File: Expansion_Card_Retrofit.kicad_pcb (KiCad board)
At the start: 2 copper layers, 24 x 27.3 mm, 40 parts, among them P1 USB_C_Plug_USB2.0, U1 RP2350_60QFN, U2 CCGM1A1, U4 W25X20CLUXIG-TR, U5 W25X20CLUXIG-TR, U6 NCP163AFCT330T2G, Y2 ABM8-272-T3

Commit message: update
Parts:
- removed D5, D6, D7, D8: 16-213SDRC/S530-A3/TR8, LED_SMD:LED_0402_1005Metric
- added C10: 100n, Capacitor_SMD:C_0402_1005Metric, F.Cu at (130.7, 141.0)
- added C100: 100n, Capacitor_SMD:C_0402_1005Metric, B.Cu at (138.9, 147.6)
- added C101: 100n, Capacitor_SMD:C_0402_1005Metric, B.Cu at (141.2, 147.5)
- added C102: 100n, Capacitor_SMD:C_0402_1005Metric, B.Cu at (141.2, 142.9)
- added C103: 100n, Capacitor_SMD:C_0402_1005Metric, B.Cu at (138.9, 146.7)
- added C104: 100n, Capacitor_SMD:C_0402_1005Metric, B.Cu at (141.2, 148.4)
- added C105: 100n, Capacitor_SMD:C_0402_1005Metric, B.Cu at (141.2, 142.0)
- added C106: 100n, Capacitor_SMD:C_0402_1005Metric, B.Cu at (138.9, 143.7)
- added C107: 1u, Capacitor_SMD:C_0402_1005Metric, B.Cu at (140.5, 145.1)
- added C108: 1u, Capacitor_SMD:C_0402_1005Metric, B.Cu at (141.6, 145.1)
- added C109: 1u, Capacitor_SMD:C_0402_1005Metric, B.Cu at (139.5, 145.1)
- added C11: 10n, Capacitor_SMD:C_0201_0603Metric, B.Cu at (130.5, 139.5)
- added C110: 1u, Capacitor_SMD:C_0402_1005Metric, B.Cu at (138.5, 145.1)
- added C111: 10n, Capacitor_SMD:C_0201_0603Metric, B.Cu at (137.3, 144.4)
- added C112: 10n, Capacitor_SMD:C_0201_0603Metric, B.Cu at (137.3, 146.0)
- added C113: 10n, Capacitor_SMD:C_0201_0603Metric, B.Cu at (142.9, 143.6)
- added C114: 10n, Capacitor_SMD:C_0201_0603Metric, B.Cu at (142.9, 144.4)
- added C115: 10n, Capacitor_SMD:C_0201_0603Metric, B.Cu at (142.9, 146.0)
- added C116: 10n, Capacitor_SMD:C_0201_0603Metric, B.Cu at (141.3, 143.8)
- added C117: 10n, Capacitor_SMD:C_0201_0603Metric, B.Cu at (141.3, 146.7)
- added C12: 100n, Capacitor_SMD:C_0402_1005Metric, B.Cu at (130.5, 140.3)
- added C13: 1u, Capacitor_SMD:C_0402_1005Metric, B.Cu at (130.5, 141.3)
- added C14: 1u, Capacitor_SMD:C_0402_1005Metric, B.Cu at (139.7, 135.4)
- added C15: 1u, Capacitor_SMD:C_0402_1005Metric, F.Cu at (139.8, 134.4)
- added C16: 10n, Capacitor_SMD:C_0201_0603Metric, B.Cu at (138.1, 149.2)
- added C17: 100n, Capacitor_SMD:C_0402_1005Metric, B.Cu at (139.2, 152.0)
- added C18: 1u, Capacitor_SMD:C_0402_1005Metric, B.Cu at (136.9, 152.1)
- added C19: 10n, Capacitor_SMD:C_0201_0603Metric, B.Cu at (139.3, 148.8)
- added C20: 10n, Capacitor_SMD:C_0201_0603Metric, B.Cu at (138.1, 148.4)
- added C21: 1u, Capacitor_SMD:C_0402_1005Metric, B.Cu at (144.2, 152.6)
- added C22: 100n, Capacitor_SMD:C_0402_1005Metric, B.Cu at (142.4, 152.0)
- added C23: 10n, Capacitor_SMD:C_0201_0603Metric, B.Cu at (142.9, 149.2)
- added C24: 10n, Capacitor_SMD:C_0201_0603Metric, B.Cu at (142.9, 148.4)
- added C25: 10n, Capacitor_SMD:C_0201_0603Metric, B.Cu at (141.3, 149.2)
- added C26: 1u, Capacitor_SMD:C_0402_1005Metric, B.Cu at (133.3, 143.5)
- added C27: 100n, Capacitor_SMD:C_0402_1005Metric, B.Cu at (136.1, 145.1)
- added C28: 10n, Capacitor_SMD:C_0201_0603Metric, B.Cu at (136.1, 143.3)
- added C29: 10n, Capacitor_SMD:C_0201_0603Metric, B.Cu at (133.3, 146.8)
- added C30: 10n, Capacitor_SMD:C_0201_0603Metric, B.Cu at (136.1, 147.2)
- added C31: 10n, Capacitor_SMD:C_0201_0603Metric, B.Cu at (136.5, 149.2)
- added C32: 10n, Capacitor_SMD:C_0201_0603Metric, B.Cu at (136.5, 148.4)
- added C33: 10n, Capacitor_SMD:C_0201_0603Metric, B.Cu at (134.5, 152.0)
- added C34: 100n, Capacitor_SMD:C_0402_1005Metric, B.Cu at (132.9, 151.9)
- added C35: 1u, Capacitor_SMD:C_0402_1005Metric, B.Cu at (133.3, 149.2)
- added C36: 10n, Capacitor_SMD:C_0201_0603Metric, B.Cu at (132.9, 140.6)
- added C37: 10n, Capacitor_SMD:C_0201_0603Metric, B.Cu at (137.3, 142.0)
- added C38: 10n, Capacitor_SMD:C_0201_0603Metric, B.Cu at (135.6, 140.4)
- added C39: 100n, Capacitor_SMD:C_0402_1005Metric, B.Cu at (140.0, 140.9)
- added C4: 4u7, Capacitor_SMD:C_0402_1005Metric, B.Cu at (139.6, 137.1)
- added C40: 1u, Capacitor_SMD:C_0402_1005Metric, B.Cu at (138.5, 141.4)
- added C41: 1u, Capacitor_SMD:C_0402_1005Metric, B.Cu at (141.9, 140.9)
- added C42: 100n, Capacitor_SMD:C_0402_1005Metric, F.Cu at (141.5, 136.2)
- added C43: 10n, Capacitor_SMD:C_0201_0603Metric, B.Cu at (140.5, 138.7)
- added C44: 10n, Capacitor_SMD:C_0201_0603Metric, B.Cu at (142.8, 139.6)
- added C45: 10n, Capacitor_SMD:C_0201_0603Metric, B.Cu at (143.2, 140.8)
- added C46: 10n, Capacitor_SMD:C_0201_0603Metric, B.Cu at (137.0, 130.6)
- added C47: 100n, Capacitor_SMD:C_0402_1005Metric, B.Cu at (135.8, 130.5)
- added C49: 10n, Capacitor_SMD:C_0201_0603Metric, F.Cu at (149.6, 151.1)
- added C5: 4u7, Capacitor_SMD:C_0402_1005Metric, B.Cu at (140.5, 137.1)
- added C50: 100n, Capacitor_SMD:C_0402_1005Metric, F.Cu at (149.6, 152.0)
- added C51: 1u, Capacitor_SMD:C_0402_1005Metric, F.Cu at (149.6, 153.0)
- added C52: 100n, Capacitor_SMD:C_0402_1005Metric, F.Cu at (111.7, 143.8)
- added C53: 10n, Capacitor_SMD:C_0201_0603Metric, B.Cu at (136.1, 139.2)
- added C54: 1u, Capacitor_SMD:C_0402_1005Metric, F.Cu at (99.2, 145.5)
- added C55: 100n, Capacitor_SMD:C_0402_1005Metric, F.Cu at (111.7, 145.8)
- added C56: 10n, Capacitor_SMD:C_0201_0603Metric, F.Cu at (99.2, 147.2)
- added C57: 1u, Capacitor_SMD:C_0402_1005Metric, B.Cu at (116.1, 146.3)
- added C58: 100n, Capacitor_SMD:C_0402_1005Metric, F.Cu at (111.7, 147.8)
- added C59: 10n, Capacitor_SMD:C_0201_0603Metric, F.Cu at (99.2, 150.7)
- added C6: 4u7, Capacitor_SMD:C_0402_1005Metric, B.Cu at (141.0, 139.8)
- added C60: 10n, Capacitor_SMD:C_0201_0603Metric, F.Cu at (99.2, 152.5)
- added C61: 10n, Capacitor_SMD:C_0201_0603Metric, F.Cu at (99.2, 154.2)
- added C62: 10n, Capacitor_SMD:C_0201_0603Metric, F.Cu at (101.7, 143.7)
- added C63: 10n, Capacitor_SMD:C_0201_0603Metric, B.Cu at (138.0, 138.8)
- added C64: 10n, Capacitor_SMD:C_0201_0603Metric, B.Cu at (134.1, 139.6)
- added C65: 1u, Capacitor_SMD:C_0402_1005Metric, B.Cu at (144.2, 144.8)
- added C66: 100n, Capacitor_SMD:C_0402_1005Metric, B.Cu at (146.9, 143.5)
- added C67: 10n, Capacitor_SMD:C_0201_0603Metric, B.Cu at (144.1, 143.2)
- added C68: 10n, Capacitor_SMD:C_0201_0603Metric, B.Cu at (146.8, 146.0)
- added C69: 10n, Capacitor_SMD:C_0201_0603Metric, B.Cu at (144.1, 146.5)
- added C70: 10n, Capacitor_SMD:C_0201_0603Metric, B.Cu at (144.1, 149.6)
- added C71: 10n, Capacitor_SMD:C_0201_0603Metric, B.Cu at (144.1, 148.0)
- added C72: 10n, Capacitor_SMD:C_0201_0603Metric, B.Cu at (146.9, 148.4)
- added C73: 100n, Capacitor_SMD:C_0402_1005Metric, B.Cu at (146.9, 150.7)
- added C74: 1u, Capacitor_SMD:C_0402_1005Metric, B.Cu at (146.9, 152.5)
- added C75: 10n, Capacitor_SMD:C_0201_0603Metric, B.Cu at (145.2, 141.2)
- added C76: 10n, Capacitor_SMD:C_0201_0603Metric, B.Cu at (147.5, 139.9)
- added C77: 10n, Capacitor_SMD:C_0201_0603Metric, B.Cu at (144.1, 140.8)
- added C78: 100n, Capacitor_SMD:C_0402_1005Metric, F.Cu at (145.8, 135.6)
- added C79: 1u, Capacitor_SMD:C_0402_1005Metric, F.Cu at (147.2, 135.8)
- added C80: 10n, Capacitor_SMD:C_0201_0603Metric, F.Cu at (144.4, 136.0)
- added C81: 1u, Capacitor_SMD:C_0402_1005Metric, F.Cu at (142.9, 135.2)
- added C82: 10n, Capacitor_SMD:C_0201_0603Metric, B.Cu at (134.5, 140.8)
- added C83: 4u7, Capacitor_SMD:C_0402_1005Metric, F.Cu at (130.0, 130.5)
- added C84: 22u, Capacitor_SMD:C_0402_1005Metric, F.Cu at (131.6, 132.9)
- added C85: 120p, Capacitor_SMD:C_0201_0603Metric, F.Cu at (132.5, 133.0)
- added C86: 4u7, Capacitor_SMD:C_0402_1005Metric, B.Cu at (130.0, 134.5)
- added C87: 120p, Capacitor_SMD:C_0201_0603Metric, B.Cu at (133.2, 132.7)
- added C88: 22u, Capacitor_SMD:C_0402_1005Metric, B.Cu at (131.6, 132.9)
- added C89: 100n, Capacitor_SMD:C_0402_1005Metric, B.Cu at (133.3, 137.9)
- added C9: 100n, Capacitor_SMD:C_0402_1005Metric, F.Cu at (130.6, 140.1)
- added C90: 1u, Capacitor_SMD:C_0402_1005Metric, B.Cu at (133.3, 136.9)
- added C91: 10n, Capacitor_SMD:C_0201_0603Metric, B.Cu at (137.3, 142.8)
- added C92: 10n, Capacitor_SMD:C_0201_0603Metric, B.Cu at (142.9, 142.0)
- added C93: 10n, Capacitor_SMD:C_0201_0603Metric, B.Cu at (137.3, 147.6)
- added C94: 10n, Capacitor_SMD:C_0201_0603Metric, B.Cu at (142.9, 146.8)
- added C95: 10n, Capacitor_SMD:C_0201_0603Metric, B.Cu at (137.3, 143.6)
- added C96: 10n, Capacitor_SMD:C_0201_0603Metric, B.Cu at (137.3, 146.8)
- added C97: 10n, Capacitor_SMD:C_0201_0603Metric, B.Cu at (142.9, 147.6)
- added C98: 10n, Capacitor_SMD:C_0201_0603Metric, B.Cu at (142.9, 142.8)
- added C99: 100n, Capacitor_SMD:C_0402_1005Metric, B.Cu at (138.9, 142.8)
- added D12: PTVS5V0Z1USK, Diode_SMD:Nexperia_DSN1608-2_1.6x0.8mm, F.Cu at (141.4, 132.3)
- added D13: PTVS5V0Z1USK, Diode_SMD:Nexperia_DSN1608-2_1.6x0.8mm, F.Cu at (141.4, 134.4)
- added JP1: Jumper_2_Open, Jumper:SolderJumper-2_P1.3mm_Open_RoundedPad1.0x1.5mm, F.Cu at (129.6, 153.3)
- added R1: 5K1, Resistor_SMD:R_0201_0603Metric, F.Cu at (139.0, 132.4)
- added R17: 5K1, Resistor_SMD:R_0201_0603Metric, F.Cu at (149.5, 137.0)
- added R18: 5K1, Resistor_SMD:R_0201_0603Metric, B.Cu at (148.0, 148.6)
- added R19: 5K1, Resistor_SMD:R_0201_0603Metric, B.Cu at (149.3, 153.9)
- added R2: 5K1, Resistor_SMD:R_0201_0603Metric, F.Cu at (135.0, 130.2)
- added R20: 5K1, Resistor_SMD:R_0201_0603Metric, B.Cu at (149.1, 148.9)
- added R21: 200R, Resistor_SMD:R_0201_0603Metric, F.Cu at (137.8, 135.8)
- added R22: 100R, Resistor_SMD:R_0201_0603Metric, F.Cu at (106.6, 152.5)
- added R23: 5K1, Resistor_SMD:R_0201_0603Metric, F.Cu at (155.3, 144.4)
- added R24: 316K, Resistor_SMD:R_0201_0603Metric, B.Cu at (132.4, 132.7)
- added R25: 200R, Resistor_SMD:R_0201_0603Metric, B.Cu at (132.2, 139.2)
- added R26: 0R, Resistor_SMD:R_0201_0603Metric, B.Cu at (132.2, 140.6)
- added R27: 0R, Resistor_SMD:R_0201_0603Metric, B.Cu at (131.9, 144.3)
- added R28: 200R, Resistor_SMD:R_0201_0603Metric, B.Cu at (131.8, 142.8)
- added R29: 0R, Resistor_SMD:R_0201_0603Metric, B.Cu at (134.6, 137.4)
- added R3: 33R, Resistor_SMD:R_0402_1005Metric, B.Cu at (139.6, 139.0)
- added R30: 0R, Resistor_SMD:R_0201_0603Metric, B.Cu at (134.1, 138.8)
- added R31: 100R, Resistor_SMD:R_0201_0603Metric, F.Cu at (109.0, 149.0)
- added R32: 0R, Resistor_SMD:R_0201_0603Metric, F.Cu at (130.6, 139.2)
- added R33: 0R, Resistor_SMD:R_0201_0603Metric, F.Cu at (130.6, 138.2)
- added R34: 0R, Resistor_SMD:R_0201_0603Metric, F.Cu at (109.0, 150.7)
- added R35: 100K, Resistor_SMD:R_0201_0603Metric, B.Cu at (132.1, 134.2)
- added R4: 5K1, Resistor_SMD:R_0201_0603Metric, F.Cu at (191.3, 113.4)
- added TH1: PTSLR06038V075, Capacitor_SMD:C_0603_1608Metric, F.Cu at (145.8, 130.3)
- added TP5: TestPoint_Small, TestPoint:TestPoint_Pad_D1.0mm, B.Cu at (151.2, 136.7)
- added TP6: TestPoint_Small, TestPoint:TestPoint_Pad_D1.0mm, B.Cu at (151.2, 138.8)
- added U3: TVS0500DRV, Package_SON:WSON-6-1EP_2x2mm_P0.65mm_EP1x1.6mm, F.Cu at (149.3, 131.1)
- added U7: TPSM82822SILR, ProjectLibrary:SIL0010D-MFG, F.Cu at (130.0, 132.6)
- added U8: TPSM82822SILR, ProjectLibrary:SIL0010D-MFG, B.Cu at (130.0, 132.6)
- added Y1: S3A2505-100.000-L-X1-R, ProjectLibrary:OSC_S3A2505-100.000-L-X1-R, B.Cu at (130.2, 137.2)
- C1, C2, C3: footprint Capacitor_SMD:C_0201_0603Metric -> Capacitor_SMD:C_0402_1005Metric
- C7, C8: value 100n -> 15p; footprint Capacitor_SMD:C_0201_0603Metric -> Capacitor_SMD:C_0402_1005Metric; moved to B.Cu
- P1: value USB_C_Plug_USB2.0 -> 1054440011
- R10, R11: value 60R4 -> 100K
- R12: value 60R4 -> 5K1
- R15: value 30R1 -> 5K1; moved to B.Cu
- R16: value 30R1 -> 0R; moved to B.Cu
- R9: value 60R4 -> 316K
- U4, U5: value W25X20CLUXIG-TR -> W25Q32RVXHJQ TR
- U6: value NCP163AFCT330T2G -> TPS7A2033PDQNR; footprint Package_CSP:WLCSP-4_0.64x0.64mm_P0.35mm -> Package_SON:Texas_X2SON-4_1x1mm_P0.65mm
- moved C8 38.4 mm to (150.4, 135.2)
- moved C7 38.0 mm to (150.2, 133.8), turned to 180 degrees
- moved D10 37.9 mm to (155.5, 141.4), turned to -90 degrees
- moved D11 36.7 mm to (154.2, 141.4), turned to 90 degrees
- moved R13 35.3 mm to (155.5, 139.5), turned to -90 degrees
- moved R14 34.2 mm to (154.2, 139.5), turned to -90 degrees
- moved R11 25.7 mm to (128.5, 133.4), turned to 90 degrees
- moved R16 24.7 mm to (135.2, 141.8), turned to -90 degrees
- moved C1 24.5 mm to (134.4, 131.0), turned to 180 degrees
- moved R10 23.9 mm to (131.9, 131.6), turned to 180 degrees
- moved U6 22.3 mm to (139.8, 135.7), turned to -90 degrees
- moved R9 21.3 mm to (133.2, 133.0), turned to 90 degrees
- moved R15 21.3 mm to (129.0, 139.8), turned to 90 degrees
- moved R12 10.2 mm to (129.7, 151.8)
- moved U5 9.53 mm to (149.1, 151.4)
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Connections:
- net /C_TX_N renamed /C_TX1_N
- net /C_TX_P renamed /C_TX1_P
- net /RX_N renamed /RX1_N
- net /RX_P renamed /RX1_P
- net Net-(D1-K) renamed /K0
- net Net-(D2-K) renamed /K1
- net Net-(D3-K) renamed /K2
- net Net-(D4-K) renamed /K3
- net Net-(U1-GPIO20) renamed /CC_CFG_CTRL_CLK
- net Net-(U1-GPIO22) renamed /CC_CFG_CTRL_VALID
- net Net-(U2C-IO_NA_A0) renamed /LED0
- C2 pad 1: /TX_N -> /TX1_N
- C3 pad 1: /TX_P -> /TX1_P
- D9 pad 2: /USB_DP -> /TX1_N
- D9 pad 4: VBUS -> /RX2_N
- D9 pad 5: /TX_P -> /TX2_N
- D9 pad 6: /TX_N -> /TX2_P
- D9 pad 7: Net-(D9-K6) -> /RX2_P
- D9 pad 8: /USB_DN -> /TX1_P
- P1 pad A10: unconnected-(P1-RX2--PadA10) -> /RX2_N
- P1 pad A11: unconnected-(P1-RX2+-PadA11) -> /RX2_P
- P1 pad A2: /TX_P -> /TX1_P
- P1 pad A3: /TX_N -> /TX1_N
- P1 pad A4: VBUS -> Net-(P1-VBUS-PadA4)
- P1 pad A5: Net-(D9-K6) -> Net-(P1-CC)
- P1 pad A9: VBUS -> Net-(P1-VBUS-PadA4)
- P1 pad B2: unconnected-(P1-TX2+-PadB2) -> /TX2_P
- P1 pad B3: unconnected-(P1-TX2--PadB3) -> /TX2_N
- P1 pad B4: VBUS -> Net-(P1-VBUS-PadA4)
- P1 pad B9: VBUS -> Net-(P1-VBUS-PadA4)
- R10 pad 1: Net-(U2C-IO_NA_A4) -> Net-(U7-FB)
- R10 pad 2: Net-(D6-K) -> GND
- R11 pad 1: Net-(U2C-IO_NA_B4) -> +2V5
- R11 pad 2: Net-(D7-K) -> /power_supply/PG
- R12 pad 1: Net-(U2C-IO_NA_A7) -> +2V5
- R12 pad 2: Net-(D8-K) -> Net-(JP1-B)
- R15 pad 1: Net-(Y1-CLK+) -> +2V5
- R15 pad 2: Net-(U2H-SER_CLK) -> Net-(Y1-ENABLE/DISABLE)
- R16 pad 1: Net-(Y1-CLK-) -> +1V
- R16 pad 2: Net-(U2H-SER_CLK_N) -> Net-(U2G-NC/VDD_SER)
- R6 pad 1: Net-(U2C-IO_NA_B0) -> /LED2
- R7 pad 1: Net-(U2C-IO_NA_A1) -> /LED4
- R8 pad 1: Net-(U2C-IO_NA_B1) -> /LED5
- R9 pad 1: Net-(U2C-IO_NA_A2) -> +2V5
- R9 pad 2: Net-(D5-K) -> Net-(U7-FB)
- U1 pad 33: Net-(U1-GPIO21) -> /GPIO21_GPOUT0
- U1 pad 35: Net-(U1-GPIO23) -> /GPIO22_GPOUT1
- U1 pad 36: unconnected-(U1-GPIO24-Pad36) -> /CC_CFG_CTRL_EN
- U1 pad 60: Net-(U1-QSPI_SS) -> Net-(JP1-B)
- U2 pad A4: Net-(U2C-IO_NA_A1) -> /LED2
- U2 pad A6: Net-(U2C-IO_NA_A4) -> /LED5
- U2 pad A8: Net-(U2C-IO_NA_A7) -> unconnected-(U2C-IO_NA_A7-PadA8)
- U2 pad B1: Net-(U1-GPIO21) -> /CC_CFG_CTRL_EN
- U2 pad B3: Net-(U2C-IO_NA_B0) -> unconnected-(U2C-IO_NA_B0-PadB3)
- U2 pad B4: Net-(U2C-IO_NA_B1) -> unconnected-(U2C-IO_NA_B1-PadB4)
- U2 pad B5: Net-(U2C-IO_NA_A2) -> /LED4
- U2 pad B6: Net-(U2C-IO_NA_B4) -> unconnected-(U2C-IO_NA_B4-PadB6)
- U2 pad D1: Net-(U1-GPIO23) -> unconnected-(U2F-IO_WC_A5-PadD1)
- U2 pad F9: +0V9 -> +1V
- U2 pad G10: +0V9 -> +1V
- U2 pad G12: +0V9 -> +1V
- U2 pad G6: +0V9 -> +1V
- U2 pad G8: +0V9 -> +1V
- U2 pad H11: +0V9 -> +1V
- U2 pad H13: +0V9 -> +1V
- U2 pad H7: +0V9 -> +1V
- U2 pad H9: +0V9 -> +1V
- U2 pad J10: +0V9 -> +1V
- U2 pad J12: +0V9 -> +1V
- U2 pad J6: +0V9 -> +1V
- U2 pad J8: +0V9 -> +1V
- U2 pad K11: +0V9 -> +1V
- U2 pad K13: +0V9 -> +1V
- U2 pad K18: unconnected-(U2D-IO_EA_A2-PadK18) -> /power_supply/PG
- U2 pad K7: +0V9 -> +1V
- U2 pad K9: +0V9 -> +1V
- U2 pad L10: +0V9 -> +1V
- U2 pad L12: +0V9 -> +1V
- U2 pad L6: +0V9 -> +1V
- U2 pad L8: +0V9 -> +1V
- U2 pad M11: +0V9 -> +1V
- U2 pad M13: +0V9 -> +1V
- U2 pad M7: +0V9 -> +1V
- U2 pad M9: +0V9 -> +1V
- U2 pad N10: +0V9 -> +1V
- U2 pad N16: unconnected-(U2G-NC-PadN16) -> Net-(U2G-NC/VDD_SER)
- U2 pad N18: +2V5 -> Net-(R27-Pad2)
- U2 pad N6: +0V9 -> +1V
- U2 pad N8: +0V9 -> +1V
- U2 pad P12: unconnected-(U2E-CLK1/IO_SB_A7-PadP12) -> /GPIO20_GPOUT0
- U2 pad P14: unconnected-(U2E-CLK2/IO_SB_A6-PadP14) -> /GPIO22_GPOUT1
- U2 pad P16: +0V9 -> +1V
- U2 pad R17: unconnected-(U2E-IO_SB_A1-PadR17) -> /C_TX2_N
- U2 pad R18: unconnected-(U2E-IO_SB_B1-PadR18) -> /C_TX2_P
- U2 pad T12: Net-(U2H-SER_CLK) -> /SER_CLK_P
- U2 pad T13: Net-(U2H-SER_CLK_N) -> /SER_CLK_N
- U2 pad T14: +2V5 -> +1V
- U2 pad T16: +0V9 -> +1V
- U2 pad T18: +2V5 -> Net-(R25-Pad2)
- U2 pad U1: unconnected-(U2B-POR_EN/IO_WA_A3-PadU1) -> /POR_EN
- U2 pad U12: +0V9 -> +1V
- U2 pad U16: GND -> Net-(U2A-GND/SER_TX1_P)
- U2 pad U17: unconnected-(U2E-IO_SB_A0-PadU17) -> /R_TX2_N
- U2 pad U18: unconnected-(U2E-IO_SB_B0-PadU18) -> /R_TX2_P
- U2 pad V12: unconnected-(U2A-SER_RTERM-PadV12) -> Net-(U2A-SER_RTERM)
- U2 pad V15: unconnected-(U2H-POR_ADJ-PadV15) -> Net-(U2H-POR_ADJ)
- U2 pad V16: GND -> Net-(U2A-GND/SER_TX1_N)
- U2 pad V17: +0V9 -> +1V
- U4 pad 1: Net-(U1-QSPI_SS) -> Net-(JP1-B)
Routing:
- net VBUS: track 2.61 -> 43.8 mm, vias 3 -> 8
- net +1V1: track 0.00 -> 28.3 mm, vias 0 -> 5
- net /TX2_N: track 0.00 -> 28.0 mm, vias 0 -> 2
- net /TX2_P: track 0.00 -> 27.6 mm, vias 0 -> 2
- net /RX2_N: track 0.00 -> 25.6 mm, vias 0 -> 2
- net /RX2_P: track 0.00 -> 24.8 mm, vias 0 -> 2
- net +1V: track 0.00 -> 19.5 mm, vias 0 -> 35
- net /HSTX_2_N: track 0.00 -> 19.0 mm, vias 0 -> 2
- net GND: track 46.5 -> 65.4 mm, vias 83 -> 98
- net +2V5: track 26.1 -> 44.4 mm, vias 46 -> 52
- net /HSTX_2_P: track 0.00 -> 18.0 mm, vias 0 -> 2
- net +0V9: track 17.0 -> 0.00 mm, vias 32 -> 0
- net /HSTX_0_N: track 0.00 -> 14.4 mm, vias 0 -> 2
- net /HSTX_3_N: track 0.00 -> 14.1 mm, vias 0 -> 1
- net /HSTX_3_P: track 0.00 -> 13.9 mm, vias 0 -> 1
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- added copper zone on B.Cu, net +1V
- added copper zone on B.Cu, net +1V1
- added copper zone on F.Cu, net +2V5
- added copper zone on B.Cu, net GND
- added copper zone on F.Cu, net GND
- added copper zone on In1.Cu, net GND
- added copper zone on In3.Cu, net GND
- added copper zone on In4.Cu, net GND
- added copper zone on In6.Cu, net GND
- added copper zone on B.Cu, net Net-(U1-VREG_LX)
- added copper zone on B.Cu, net VBUS
- added copper zone on F.Cu, net VBUS
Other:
- copper layers 2 -> 8

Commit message: first routing
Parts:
- removed C49: 10n, Capacitor_SMD:C_0201_0603Metric
- removed C50: 100n, Capacitor_SMD:C_0402_1005Metric
- removed C51: 1u, Capacitor_SMD:C_0402_1005Metric
- removed JP1: Jumper_2_Open, Jumper:SolderJumper-2_P1.3mm_Open_RoundedPad1.0x1.5mm
- removed R18, R19, R20: 5K1, Resistor_SMD:R_0201_0603Metric
- removed U5: W25Q32RVXHJQ TR, Package_SON:Winbond_USON-8-1EP_3x2mm_P0.5mm_EP0.2x1.6mm
- added D14: PTVS5V0Z1USK, Diode_SMD:Nexperia_DSN1608-2_1.6x0.8mm, F.Cu at (149.6, 149.3)
- added D15: PTVS5V0Z1USK, Diode_SMD:Nexperia_DSN1608-2_1.6x0.8mm, B.Cu at (148.3, 150.5)
- added D16: PTVS5V0Z1USK, Diode_SMD:Nexperia_DSN1608-2_1.6x0.8mm, B.Cu at (148.3, 148.4)
- added D5: 16-213SDRC/S530-A3/TR8, LED_SMD:LED_0402_1005Metric, B.Cu at (135.3, 153.7)
- added D6: 16-213SDRC/S530-A3/TR8, LED_SMD:LED_0402_1005Metric, B.Cu at (133.4, 153.7)
- added J1: Conn_02x02_Odd_Even, Connector_PinHeader_1.00mm:PinHeader_2x02_P1.00mm_Horizontal, F.Cu at (130.4, 151.7)
- added J3: 5024302030, Connector_Molex:Molex_SlimStack_502430-2010_2x10_P0.40mm_Vertical, F.Cu at (150.3, 140.5)
- added J4: Conn_02x02_Odd_Even, Connector_PinHeader_1.00mm:PinHeader_2x02_P1.00mm_Horizontal, F.Cu at (151.1, 151.7)
- added R36: 60R4, Resistor_SMD:R_0201_0603Metric, F.Cu at (135.5, 154.1)
- added R37: 60R4, Resistor_SMD:R_0201_0603Metric, F.Cu at (133.6, 154.1)
- added R38: 0R, Resistor_SMD:R_0201_0603Metric, B.Cu at (149.9, 139.7)
- added R39: 0R, Resistor_SMD:R_0201_0603Metric, B.Cu at (149.9, 138.9)
- C14: moved to F.Cu
- C52, D10, D11, R12, R22, R31, R34, R4: moved to B.Cu
- moved R4 62.0 mm to (135.3, 139.9), turned to 90 degrees
- moved C61 52.1 mm to (146.3, 131.8), turned to -90 degrees
- moved C60 51.8 mm to (147.5, 133.6), turned to 180 degrees
- moved C59 50.6 mm to (147.7, 136.3), turned to 180 degrees
- moved C56 50.2 mm to (147.8, 134.8), turned to 90 degrees
- moved C54 47.1 mm to (144.4, 131.9), turned to -90 degrees
- moved C62 43.1 mm to (143.0, 131.3)
- moved R34 40.4 mm to (147.8, 139.6), turned to 180 degrees
- moved C58 37.3 mm to (145.5, 132.0), turned to -90 degrees
- moved C57 36.7 mm to (149.7, 131.4), turned to 90 degrees
- moved C55 34.2 mm to (144.3, 135.8), turned to 90 degrees
- moved R22 32.3 mm to (135.3, 137.7), turned to 90 degrees
- moved R31 28.4 mm to (133.9, 135.2)
- moved C52 23.5 mm to (133.9, 136.0), turned to 180 degrees
- moved R17 22.9 mm to (130.4, 149.6), turned to -90 degrees
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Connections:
- net Net-(JP1-B) renamed /~{FLASH_CS}
- net Net-(U1-QSPI_SCLK) renamed /FLASH_CLK
- net Net-(U1-QSPI_SD0) renamed /FLASH_S0
- net Net-(U1-QSPI_SD1) renamed /FLASH_S1
- net Net-(U1-QSPI_SD2) renamed /FLASH_S2
- net Net-(U1-QSPI_SD3) renamed /FLASH_S3
- R6 pad 1: /LED2 -> /LED1
- R7 pad 1: /LED4 -> /LED2
- R8 pad 1: /LED5 -> /LED3
- U1 pad 33: /GPIO21_GPOUT0 -> unconnected-(U1-GPIO21-Pad33)
- U1 pad 35: /GPIO22_GPOUT1 -> /GPIO23_GPOUT1
- U2 pad A12: unconnected-(U2C-IO_NB_B4-PadA12) -> /LED2
- U2 pad A14: unconnected-(U2C-IO_NB_B7-PadA14) -> /LED4
- U2 pad A3: /LED0 -> unconnected-(U2C-IO_NA_A0-PadA3)
- U2 pad A4: /LED2 -> unconnected-(U2C-IO_NA_A1-PadA4)
- U2 pad A6: /LED5 -> unconnected-(U2C-IO_NA_A4-PadA6)
- U2 pad A8: unconnected-(U2C-IO_NA_A7-PadA8) -> /LED0
- U2 pad A9: unconnected-(U2C-IO_NB_B0-PadA9) -> /LED1
- U2 pad B12: unconnected-(U2C-IO_NB_A4-PadB12) -> /LED3
- U2 pad B14: unconnected-(U2C-IO_NB_A7-PadB14) -> /LED5
- U2 pad B5: /LED4 -> unconnected-(U2C-IO_NA_A2-PadB5)
- U2 pad C17: unconnected-(U2D-IO_EB_B4-PadC17) -> /RX1
- U2 pad C18: unconnected-(U2D-IO_EB_A4-PadC18) -> /RX0
- U2 pad D17: unconnected-(U2D-IO_EB_B2-PadD17) -> /TX1
- U2 pad D18: unconnected-(U2D-IO_EB_A2-PadD18) -> /TX0
- U2 pad E3: unconnected-(U2F-IO_WC_A4-PadE3) -> /IO_P
- U2 pad E4: unconnected-(U2F-IO_WC_B4-PadE4) -> /IO_N
- U2 pad L3: /TX1 -> unconnected-(U2F-IO_WB_A2-PadL3)
- U2 pad L4: /RX1 -> unconnected-(U2F-IO_WB_B2-PadL4)
- U2 pad M3: /TX0 -> unconnected-(U2F-IO_WB_A1-PadM3)
- U2 pad M4: /RX0 -> unconnected-(U2F-IO_WB_B1-PadM4)
- U2 pad P12: /GPIO20_GPOUT0 -> /GPIO23_GPOUT1
- U2 pad P14: /GPIO22_GPOUT1 -> unconnected-(U2E-CLK2/IO_SB_A6-PadP14)
- U2 pad U4: GND -> /CFG_MD2/IO_WA_A1
- U2 pad V4: GND -> /CFG_MD3/IO_WA_B1
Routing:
- net /~{RST}: track 0.57 -> 65.9 mm, vias 1 -> 2
- net GND: track 65.4 -> 107.6 mm, vias 98 -> 108
- net /~{FLASH_CS}: track 2.04 -> 38.2 mm, vias 0 -> 2
- net /RUN: track 0.00 -> 33.0 mm, vias 0 -> 1
- net /TX1: track 0.57 -> 31.0 mm, vias 1 -> 2
- net /CC_CFG_CTRL_VALID: track 0.57 -> 26.7 mm, vias 1 -> 2
- net +2V5: track 44.4 -> 70.4 mm, vias 52 -> 54
- net /RX1: track 0.57 -> 25.5 mm, vias 1 -> 2
- net Net-(U2B-IO_WA_B2/CFG_DONE): track 3.13 -> 26.9 mm, vias 0 -> 2
- net /RX0: track 0.57 -> 24.1 mm, vias 1 -> 2
- net /TX0: track 0.57 -> 23.9 mm, vias 1 -> 2
- net /CC_CFG_CTRL_EN: track 0.57 -> 21.3 mm, vias 1 -> 2
- net /TCK: track 0.57 -> 18.4 mm, vias 1 -> 2
- net /CC_CFG_CTRL_CLK: track 0.57 -> 18.1 mm, vias 1 -> 2
- net Net-(U2B-IO_WA_A2/~{CFG_FAILED}): track 2.17 -> 19.2 mm, vias 0 -> 4
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
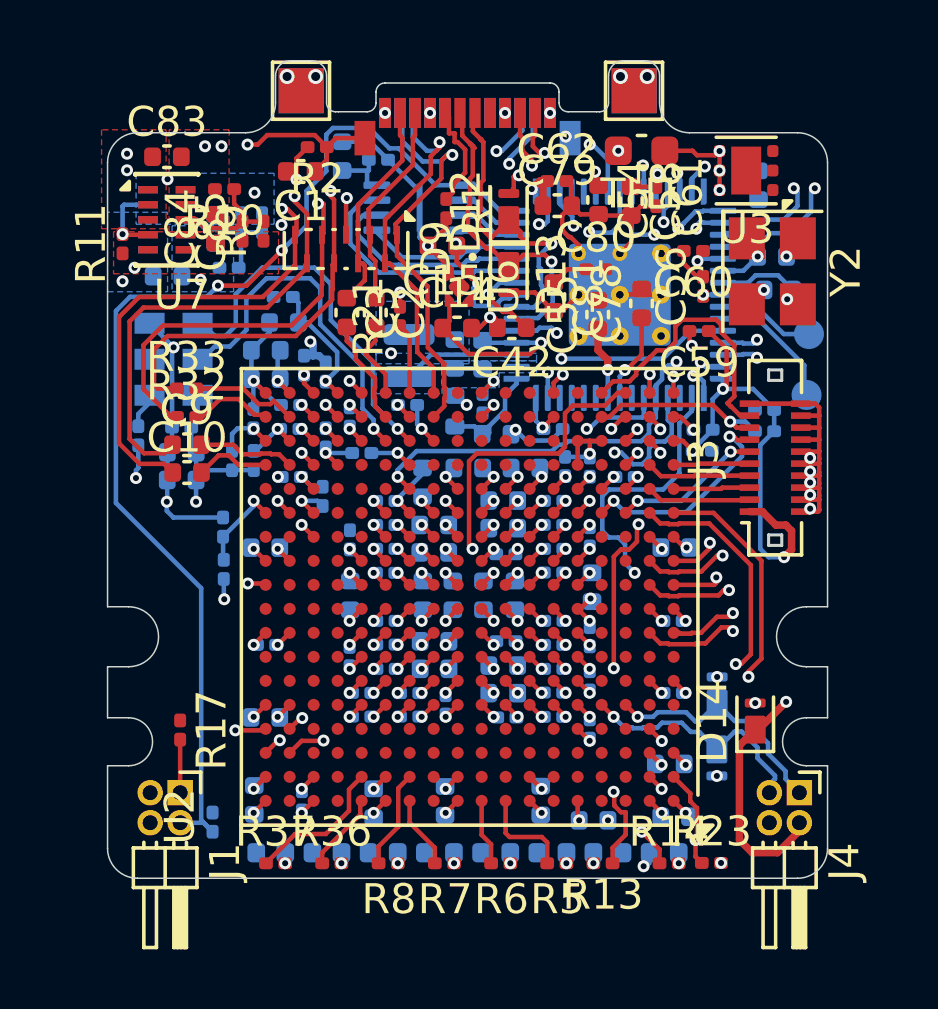
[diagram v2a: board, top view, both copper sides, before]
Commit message: Layout and add sensor
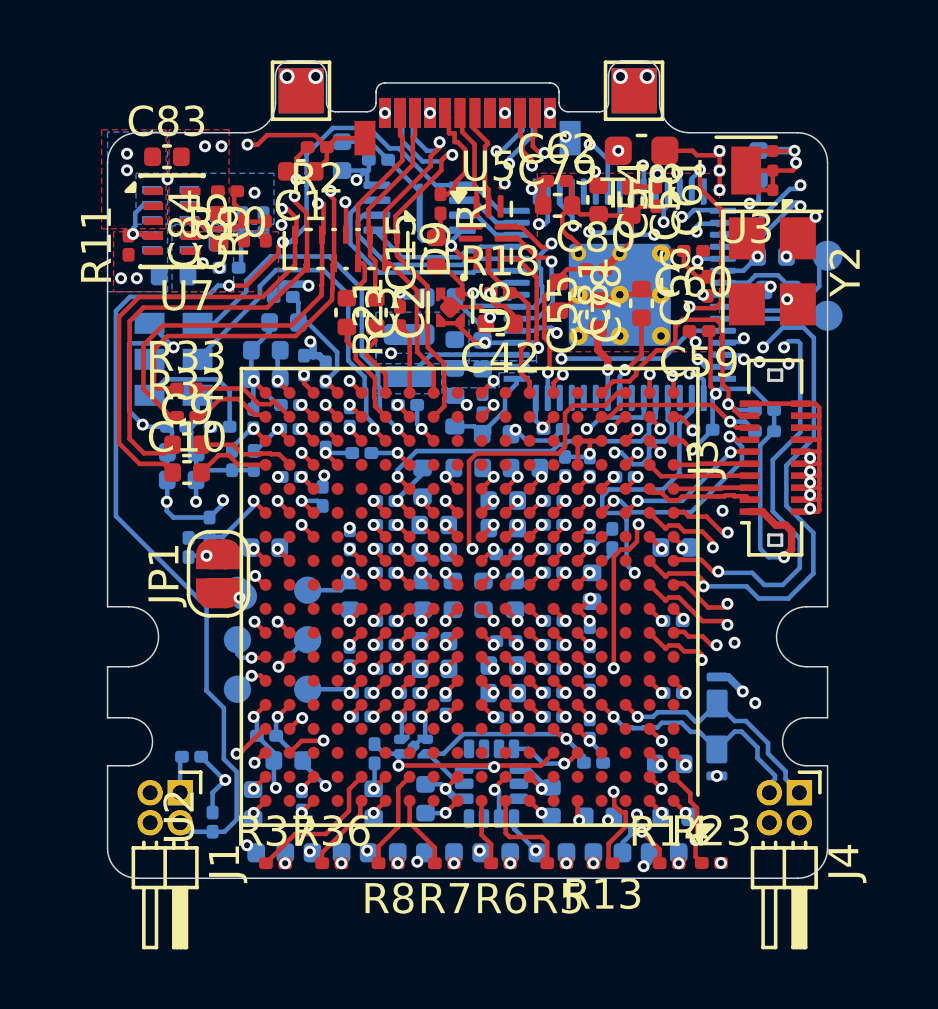
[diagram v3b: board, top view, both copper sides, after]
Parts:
- removed D12, D13, D14: PTVS5V0Z1USK, Diode_SMD:Nexperia_DSN1608-2_1.6x0.8mm
- added JP1: Jumper_2_Small_Open, Jumper:SolderJumper-2_P1.3mm_Open_RoundedPad1.0x1.5mm, F.Cu at (131.7, 144.4)
- added MK1: CMM-4737DT-26386-TR, Sensor_Audio:ST_HLGA-6_3.76x4.72mm_P1.65mm, B.Cu at (133.5, 146.6)
- added R18: 5K1, Resistor_SMD:R_0201_0603Metric, F.Cu at (141.1, 135.0)
- added R19: 5K1, Resistor_SMD:R_0201_0603Metric, B.Cu at (136.9, 150.4)
- added R20: 5K1, Resistor_SMD:R_0201_0603Metric, B.Cu at (144.2, 150.7)
- added U10: TMP110D, Package_SON:Texas_X2SON-5_0.8x0.8mm_P0.48mm, B.Cu at (138.2, 150.2)
- added U5: USB3740B-AI2, Package_DFN_QFN:UQFN-10_1.3x1.8mm_P0.4mm, F.Cu at (140.7, 133.0)
- added U9: ISM330DHCX, Package_LGA:LGA-14_3x2.5mm_P0.5mm_LayoutBorder3x4y, B.Cu at (140.8, 151.4)
- C14, R17: moved to B.Cu
- U4: value W25Q32RVXHJQ TR -> W25Q16JLUXIG TR
- moved C76 4.19 mm to (144.8, 143.2), turned to 90 degrees
- moved C29 3.03 mm to (133.3, 149.8)
- moved R15 2.74 mm to (131.8, 139.5), turned to 0 degrees
- moved TP6 2.73 mm to (152.0, 135.8)
- moved TP5 2.68 mm to (152.0, 133.8)
- moved C35 1.63 mm to (134.0, 150.6)
- moved R27 1.38 mm to (130.7, 143.5)
- moved C14 1.16 mm to (139.1, 135.2), turned to 180 degrees
- moved R17 0.97 mm to (130.8, 150.5), turned to 180 degrees
- moved U6 0.74 mm to (139.4, 135.5)
- moved C57 0.67 mm to (149.7, 130.8)
- moved C17 0.65 mm to (138.6, 151.9)
- moved R28 0.45 mm to (131.4, 142.8)
- moved C42 0.41 mm to (141.1, 136.1)
- moved C22 0.36 mm to (142.8, 152.0)
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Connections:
- net /K5 renamed /K8
- J4 pad 2: +2V5 -> GND
- P1 pad A6: /USB_DN -> /C_USB_DP
- P1 pad A7: /USB_DP -> /C_USB_DN
- U2 pad B8: unconnected-(U2C-IO_NA_B7-PadB8) -> /IMU_INT2
- U2 pad C5: unconnected-(U2C-IO_NA_B2-PadC5) -> /IMU_INT1
- U2 pad C6: unconnected-(U2C-IO_NA_A3-PadC6) -> /SDA0
- U2 pad D6: unconnected-(U2C-IO_NA_B3-PadD6) -> /SCL0
- U2 pad F18: unconnected-(U2D-IO_EB_A0-PadF18) -> /MIC_CLK
- U2 pad G17: unconnected-(U2D-IO_EA_B7-PadG17) -> /MIC_LR
- U2 pad G18: unconnected-(U2D-IO_EA_A7-PadG18) -> /MIC_DOUT
- U2 pad H1: /HSTX_3_P -> /HSTX_1_P
- U2 pad H2: /HSTX_3_N -> /HSTX_1_N
- U2 pad L1: /HSTX_1_P -> /HSTX_0_P
- U2 pad L2: /HSTX_1_N -> /HSTX_0_N
- U2 pad N1: /HSTX_0_P -> /HSTX_3_P
- U2 pad N2: /HSTX_0_N -> /HSTX_3_N
- U2 pad V7: unconnected-(U2E-IO_SA_B3-PadV7) -> /D_EN
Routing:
- net GND: track 107.6 -> 129.1 mm, vias 108 -> 119
- net /HSTX_1_P: track 5.08 -> 23.7 mm
- net /HSTX_1_N: track 7.10 -> 24.7 mm
- net /HSTX_0_N: track 8.78 -> 23.4 mm, vias 2 -> 3
- net +3V3: track 6.79 -> 21.0 mm, vias 4 -> 3
- net /HSTX_0_P: track 9.37 -> 21.9 mm, vias 2 -> 3
- net +2V5: track 70.4 -> 80.5 mm, vias 54 -> 68
- net /SCL0: track 0.00 -> 8.36 mm, vias 0 -> 1
- net /SDA0: track 0.00 -> 7.90 mm, vias 0 -> 2
- net /USB_DN: track 11.1 -> 4.66 mm
- net /USB_DP: track 10.6 -> 4.89 mm
- net /D_EN: track 0.00 -> 5.37 mm
- net /HSTX_2_N: track 18.1 -> 13.9 mm
- net /C_USB_DN: track 0.00 -> 3.44 mm
- net /C_USB_DP: track 0.00 -> 3.34 mm
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- added copper zone on In5.Cu, net +2V5
- added copper zone on In2.Cu, net GND
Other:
- board text added: "0.1524 mm / 0.1016 mm"
- board text added: "0.2000 mm"
- board text added: "0.7964 mm"
- board text added: "8"
- board text added: "ENIG"
- board text added: "Yes"
